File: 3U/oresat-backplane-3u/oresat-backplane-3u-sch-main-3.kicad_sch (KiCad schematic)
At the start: 30 parts

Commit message: Fixed libraries and footprints, synced sch and pcb (sorry Jacob).
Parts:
- C20.1, C20.2, R20.5, R20.6: footprint oresat-passives:0603-SMALL -> oresat-passives:0603-C-NOSILK
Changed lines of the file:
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@@
 			)
 		)
-		(property "Footprint" "oresat-backplane-2u:"
+		(property "Footprint" ""
 			(at 180.34 135.89 0)
 			(effects
@@
 			)
 		)
-		(property "Footprint" "oresat-backplane-2u:"
+		(property "Footprint" ""
 			(at 219.71 135.89 0)
 			(effects
@@
 			)
 		)
-		(property "Footprint" "oresat-backplane-2u:"
+		(property "Footprint" ""
 			(at 257.81 135.89 0)
 			(effects
@@
 			)
 		)
-		(property "Footprint" "oresat-backplane-2u:"
+		(property "Footprint" ""
 			(at 143.51 135.89 0)
 			(effects
@@
 			)
 		)
-		(property "Footprint" "oresat-backplane-2u:"
+		(property "Footprint" ""
 			(at 143.51 257.81 0)
 			(effects
@@
 			)
 		)
-		(property "Footprint" "oresat-passives:0603-SMALL"
+		(property "Footprint" "oresat-passives:0603-C-NOSILK"
 			(at 326.39 246.38 0)
 			(effects
@@
 			)
 		)
-		(property "Footprint" "oresat-backplane-2u:"
+		(property "Footprint" ""
 			(at 326.39 210.82 0)
 			(effects
@@
 			)
 		)
-		(property "Footprint" "oresat-backplane-2u:"
+		(property "Footprint" ""
 			(at 294.64 257.81 0)
 			(effects
@@
 			)
 		)
-		(property "Footprint" "oresat-backplane-2u:"
+		(property "Footprint" ""
 			(at 297.18 135.89 0)
 			(effects
@@
 			)
 		)
-		(property "Footprint" "oresat-backplane-2u:"
+		(property "Footprint" ""
 			(at 217.17 257.81 0)
 			(effects
@@
 			)
 		)
-		(property "Footprint" "oresat-passives:0603-SMALL"
+		(property "Footprint" "oresat-passives:0603-C-NOSILK"
 			(at 353.06 219.71 90)
 			(effects
@@
 			)
 		)
-		(property "Footprint" "oresat-backplane-2u:"
+		(property "Footprint" ""
 			(at 326.39 252.73 0)
 			(effects
@@
 			)
 		)
-		(property "Footprint" "oresat-backplane-2u:"
+		(property "Footprint" ""
 			(at 256.54 257.81 0)
 			(effects
@@
 			)
 		)
-		(property "Footprint" "oresat-passives:0603-SMALL"
+		(property "Footprint" "oresat-passives:0603-C-NOSILK"
 			(at 353.06 227.33 90)
 			(effects
@@
 			)
 		)
-		(property "Footprint" "oresat-backplane-2u:"
+		(property "Footprint" ""
 			(at 180.34 257.81 0)
 			(effects
@@
 			)
 		)
-		(property "Footprint" "oresat-backplane-2u:"
+		(property "Footprint" ""
 			(at 335.28 135.89 0)
 			(effects
@@
 			)
 		)
-		(property "Footprint" "oresat-passives:0603-SMALL"
+		(property "Footprint" "oresat-passives:0603-C-NOSILK"
 			(at 326.39 204.47 0)
 			(effects

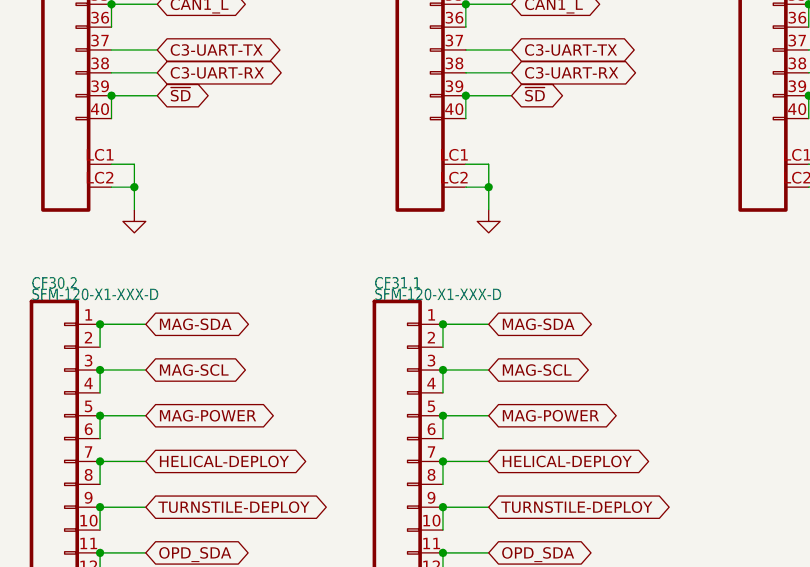
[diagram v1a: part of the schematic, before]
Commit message: Connectors laid out, unrouted
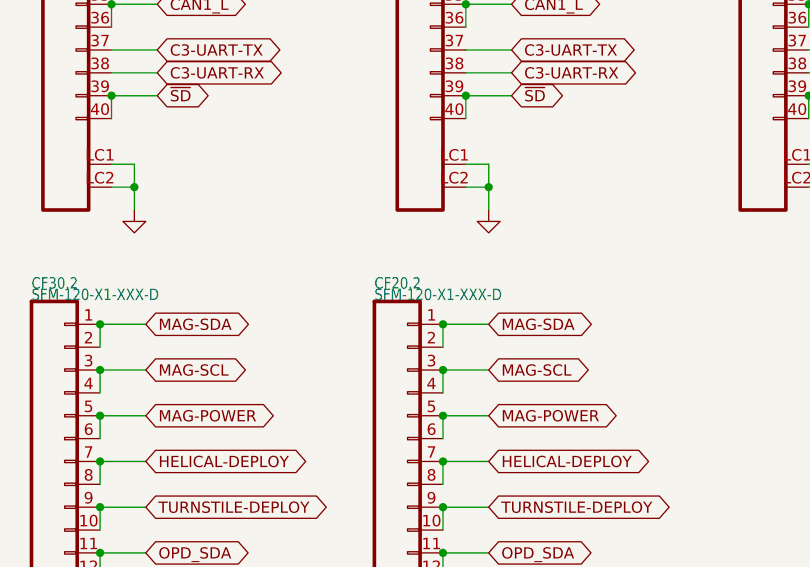
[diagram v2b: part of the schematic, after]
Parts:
- renumbered CF31.1 to CF20.2
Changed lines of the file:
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@@
 		(on_board yes)
 		(dnp no)
-		(property "Reference" "CF31.1"
+		(property "Reference" "CF20.2"
 			(at 284.48 144.78 0)
 			(effects
@@
 			(project "oresat-backplane-3u"
 				(path "/300eeac4-6caf-4310-939c-5dc51539800c/96e408d0-3df4-4718-9b55-8aaf33703ff6"
-					(reference "CF31.1")
+					(reference "CF20.2")
 					(unit 1)
 				)

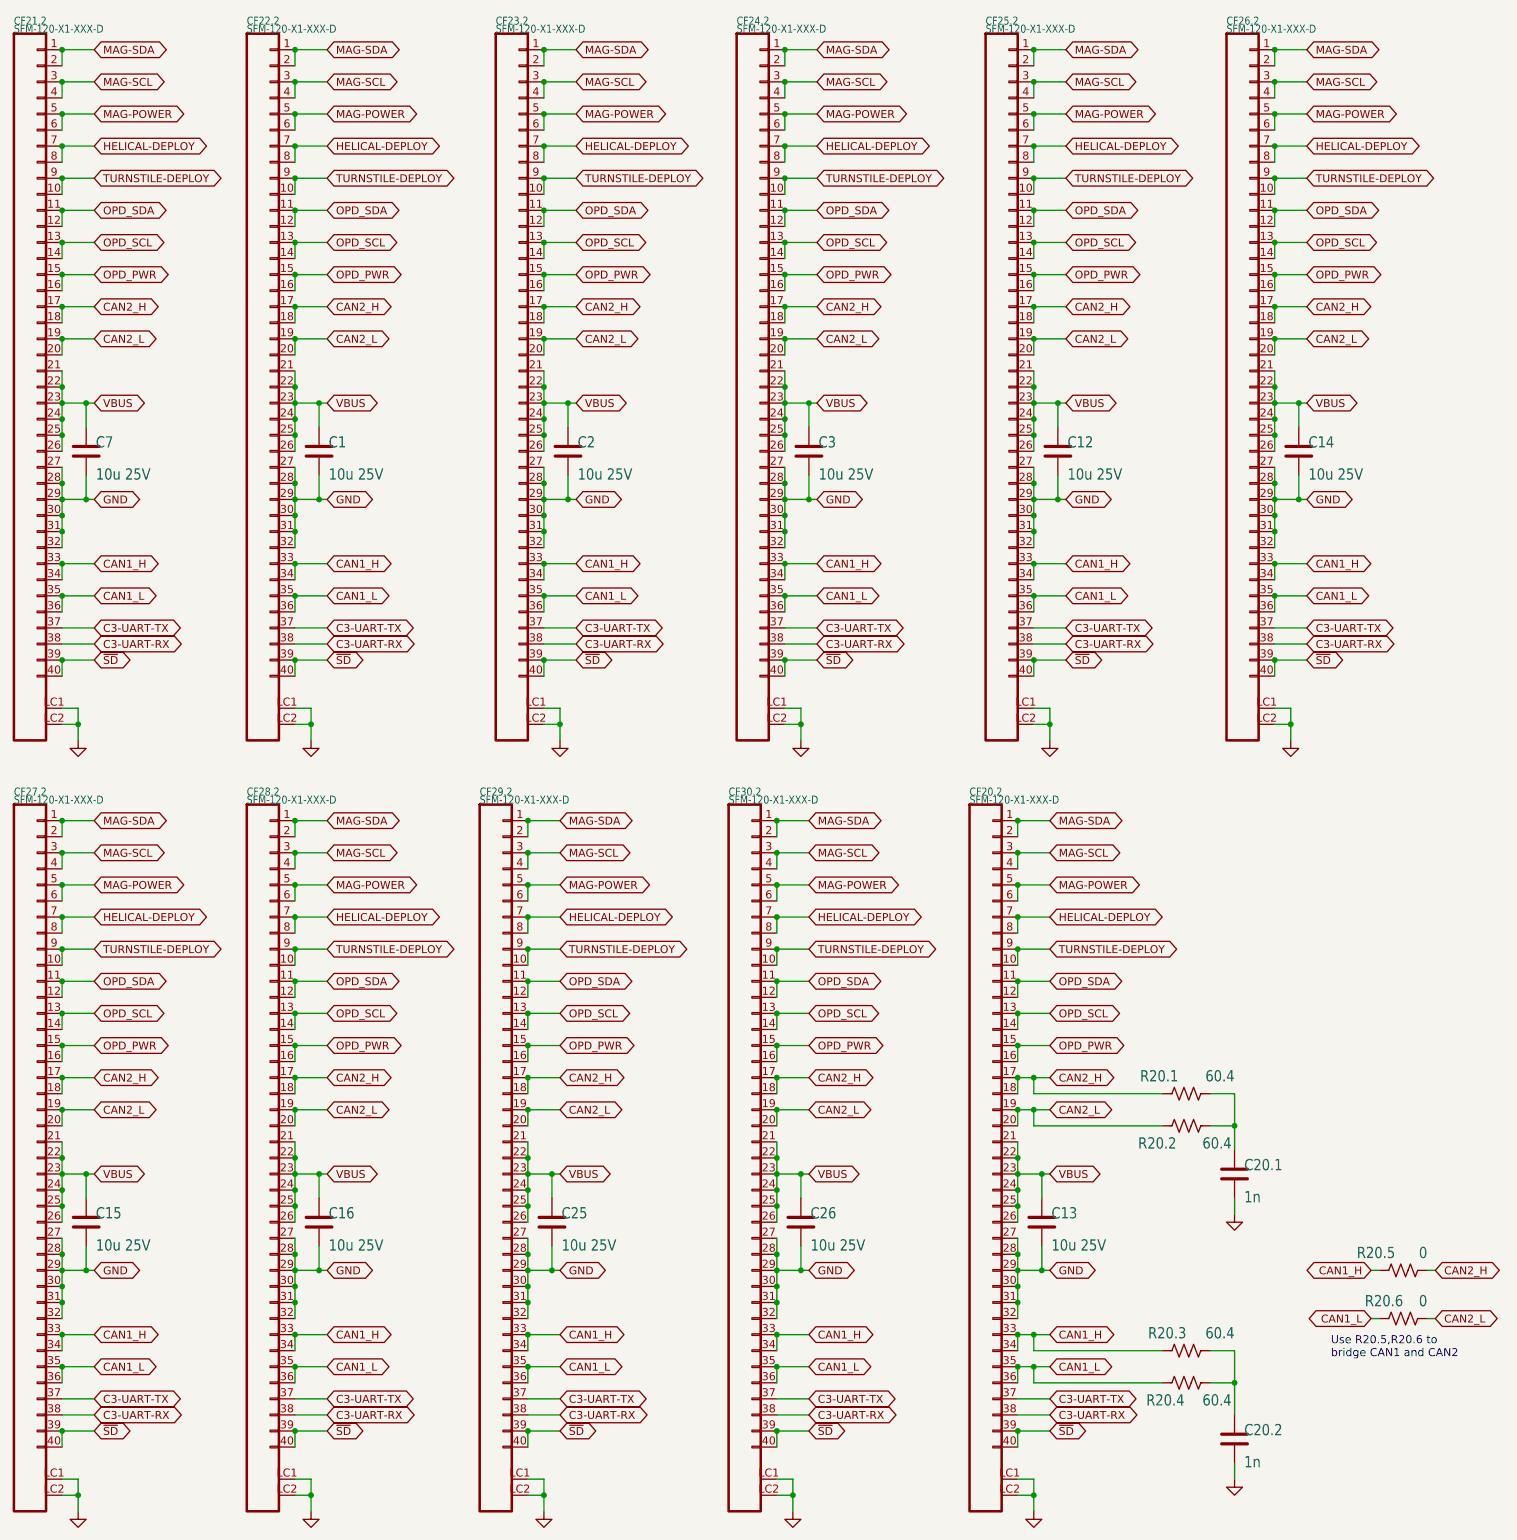
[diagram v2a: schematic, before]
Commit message: Can lines on back - need to move can resistors to front & add b.side solder mask
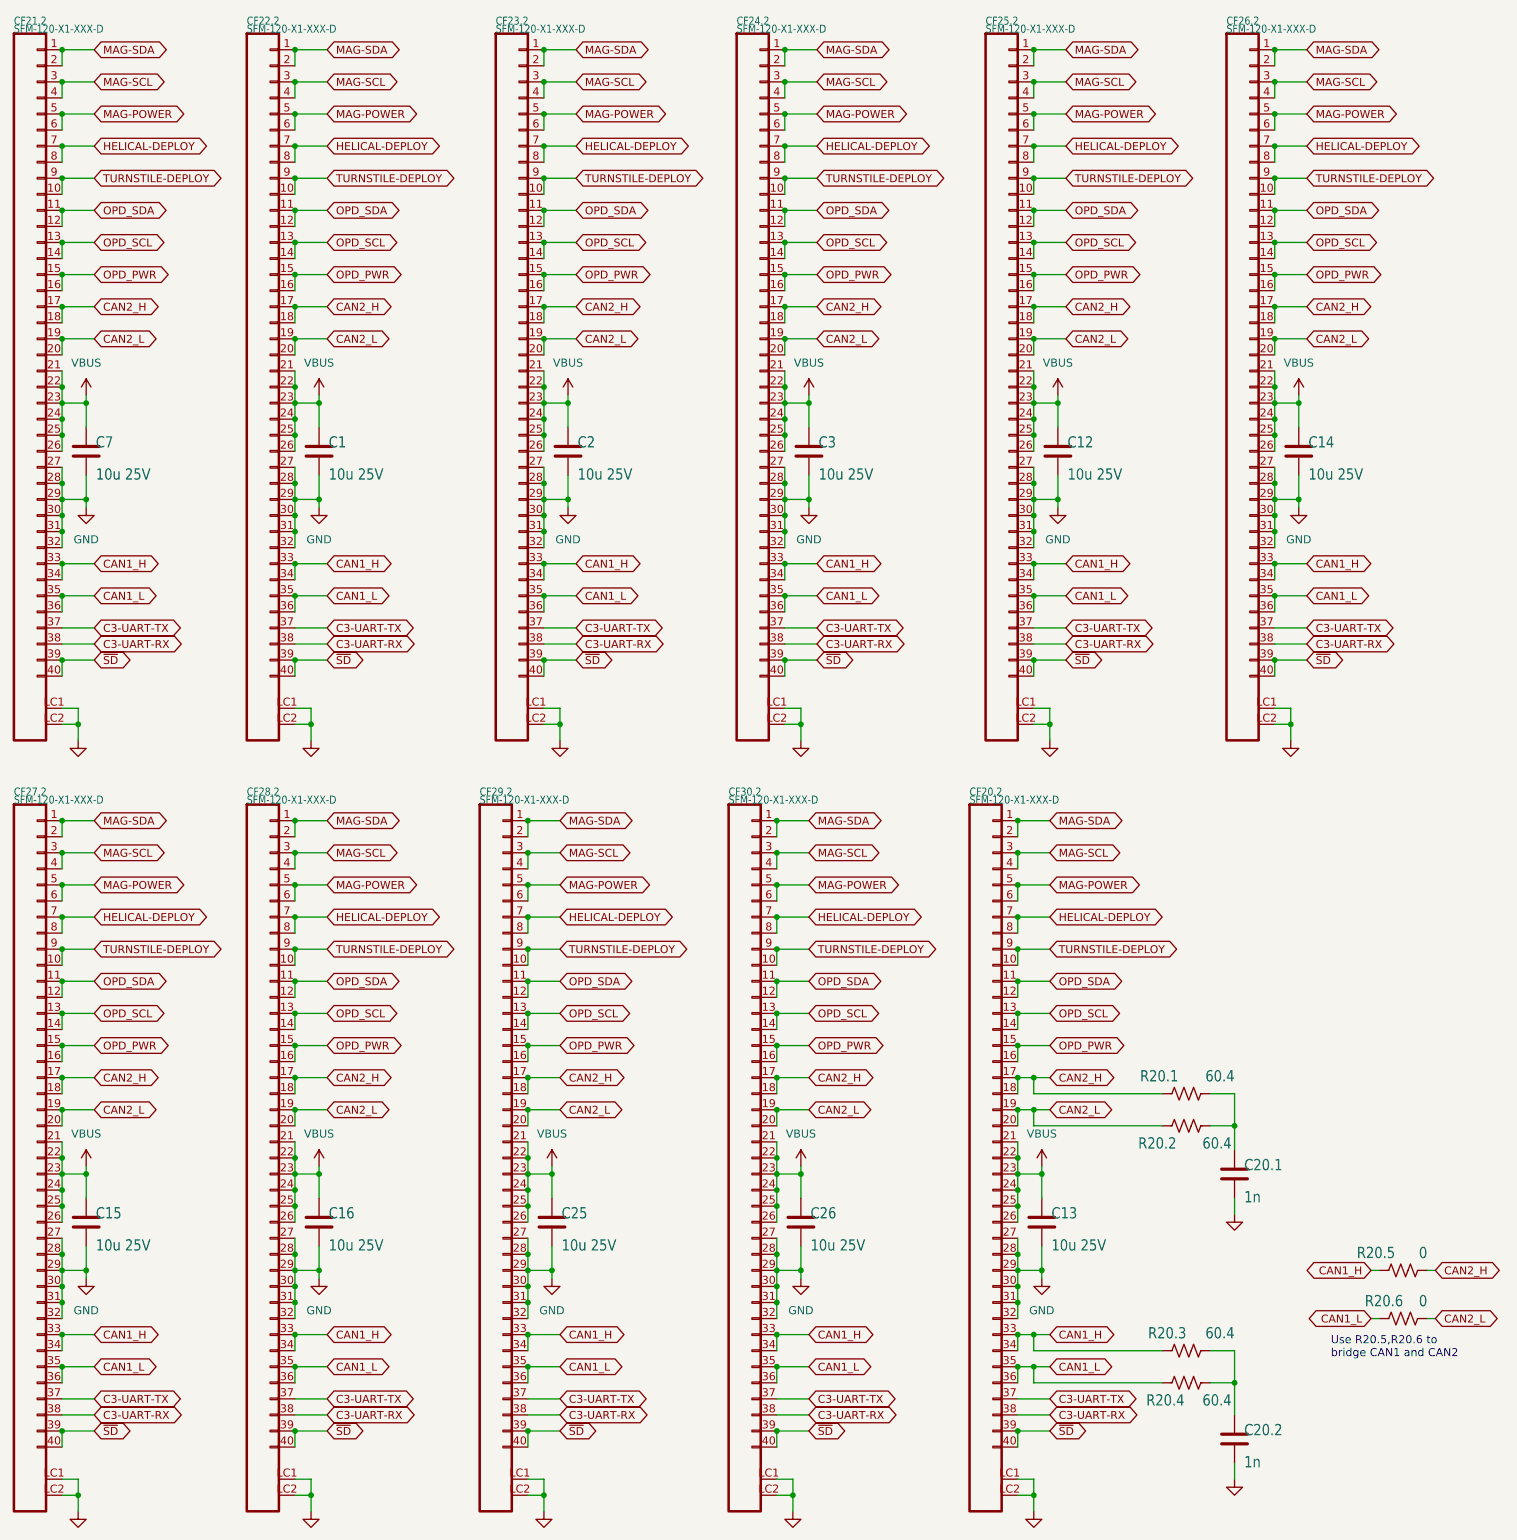
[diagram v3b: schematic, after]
